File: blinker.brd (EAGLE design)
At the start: 21.3 x 22.5 mm, 13 parts, among them U1 ATTINY85-20S, U2 L3GD20H, U3 MIC5504-3.3YM5-T5

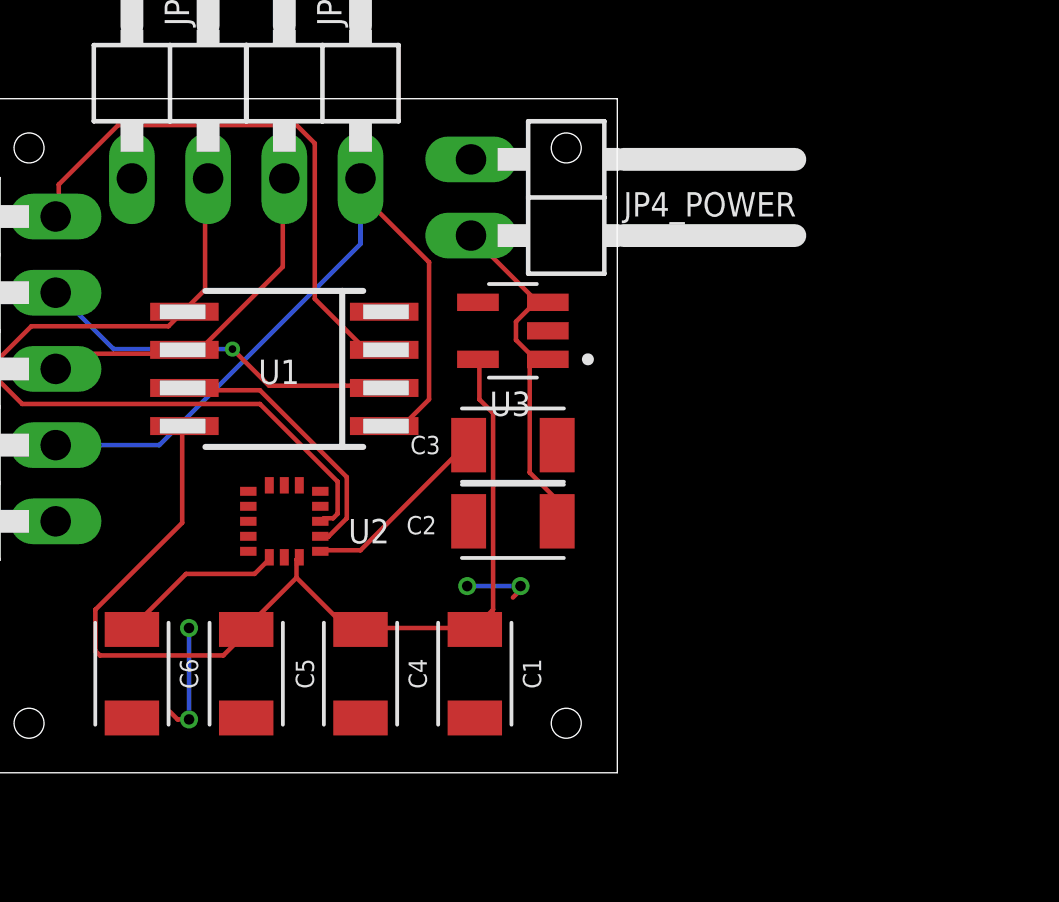
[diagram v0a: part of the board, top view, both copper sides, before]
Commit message: fix gyro connections
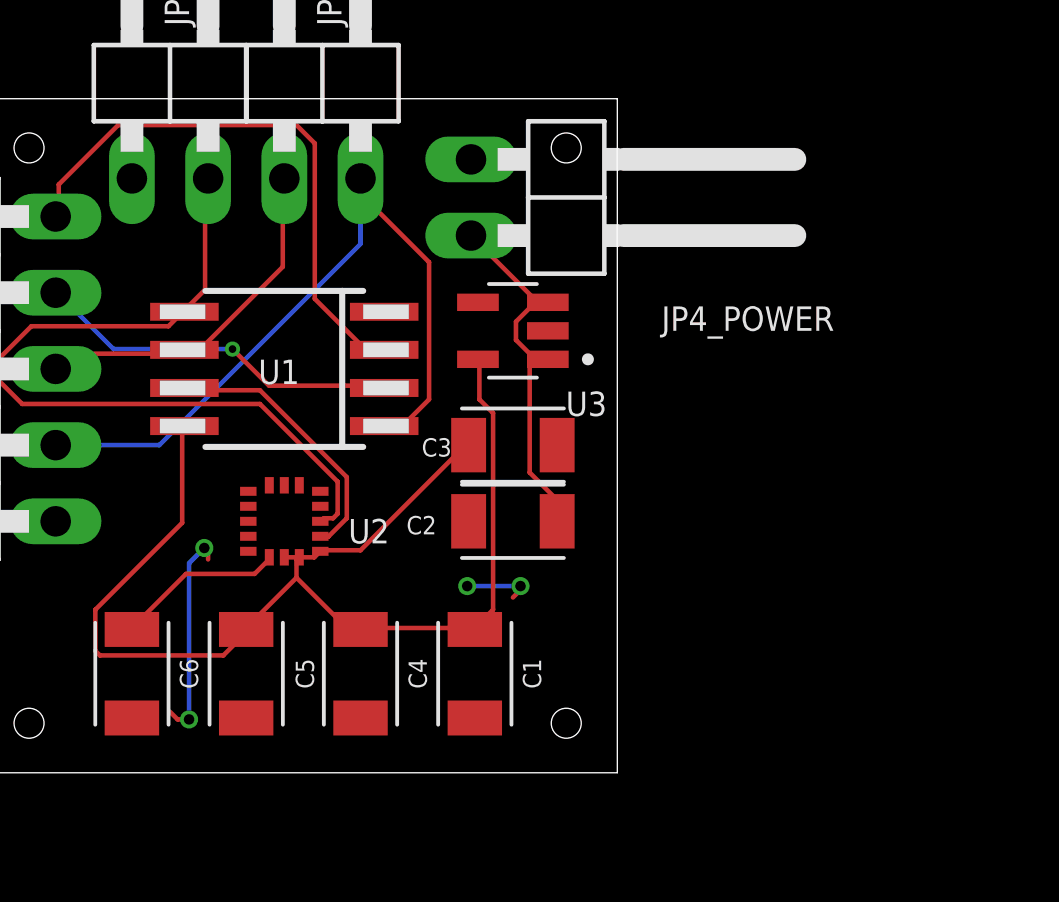
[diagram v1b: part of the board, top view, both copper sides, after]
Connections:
- removed net N$2: C3.1, U2.1
- net +3V3: now also C3.1, U2.1, U2.15
- net GND: no longer U2.15
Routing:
- net +3V3: track 33.5 -> 41.2 mm
- net N$2: track 6.40 -> 0.00 mm
- net GND: track 6.12 -> 9.43 mm
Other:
- board text added: "PB1"
- board text added: "PB3"
- board text added: "PB4"
- board text added: "PB5"
- board text added: "SDA"
- board text added: "SLC"
- board text added: "VCC"
